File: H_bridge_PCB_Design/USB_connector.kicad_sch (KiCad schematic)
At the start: 11 parts, among them J1 TMS-102-21-G-S, P1 USB_C_Plug_USB2.0, Q7 BC817, Q8 BC817, U7 CH340C

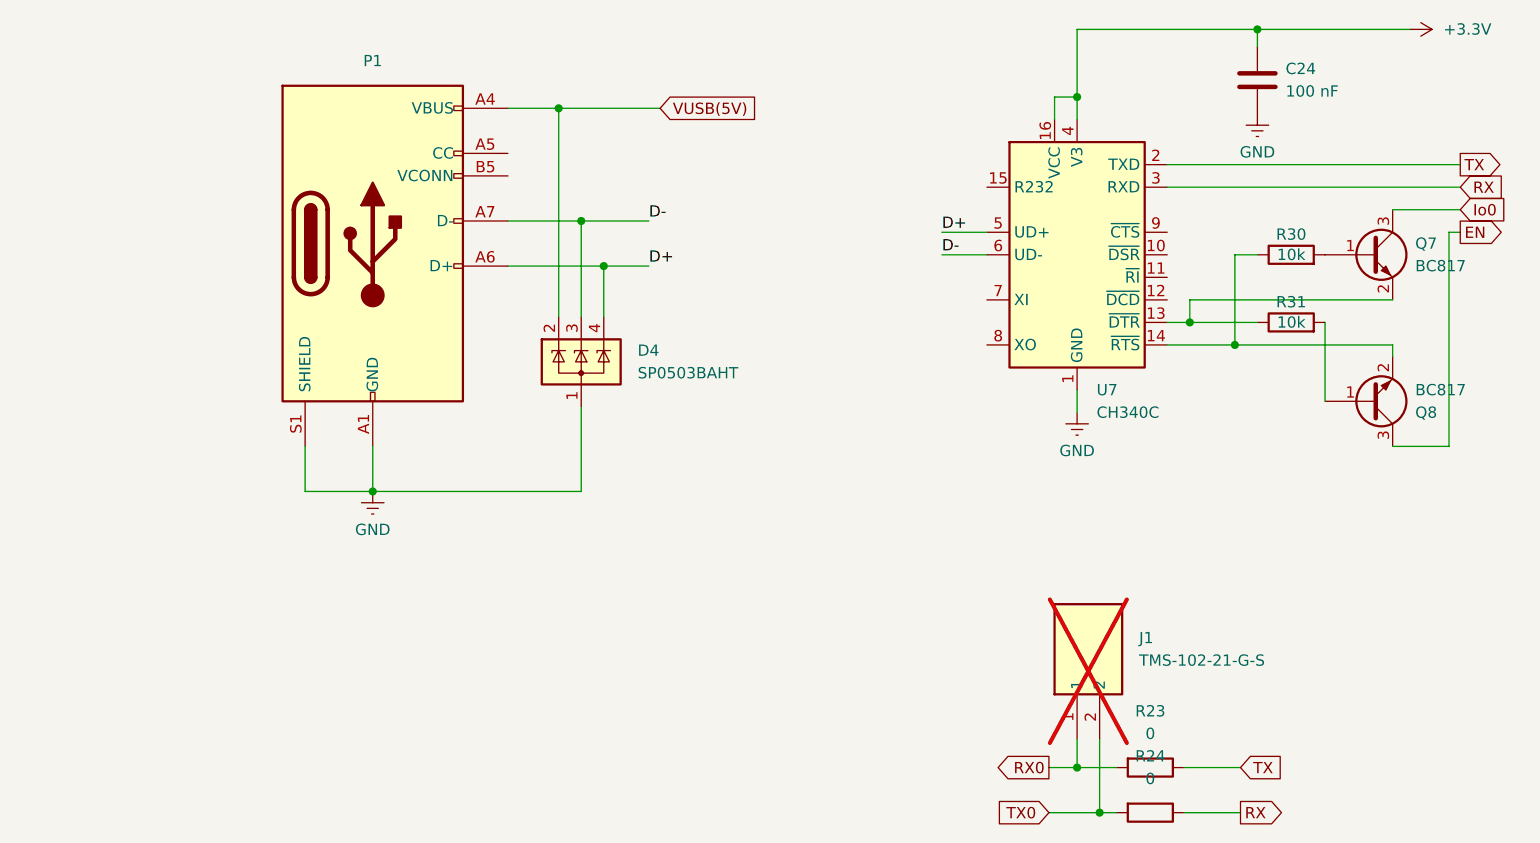
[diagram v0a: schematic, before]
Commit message: Interrupt for PWM and unipolar modulation
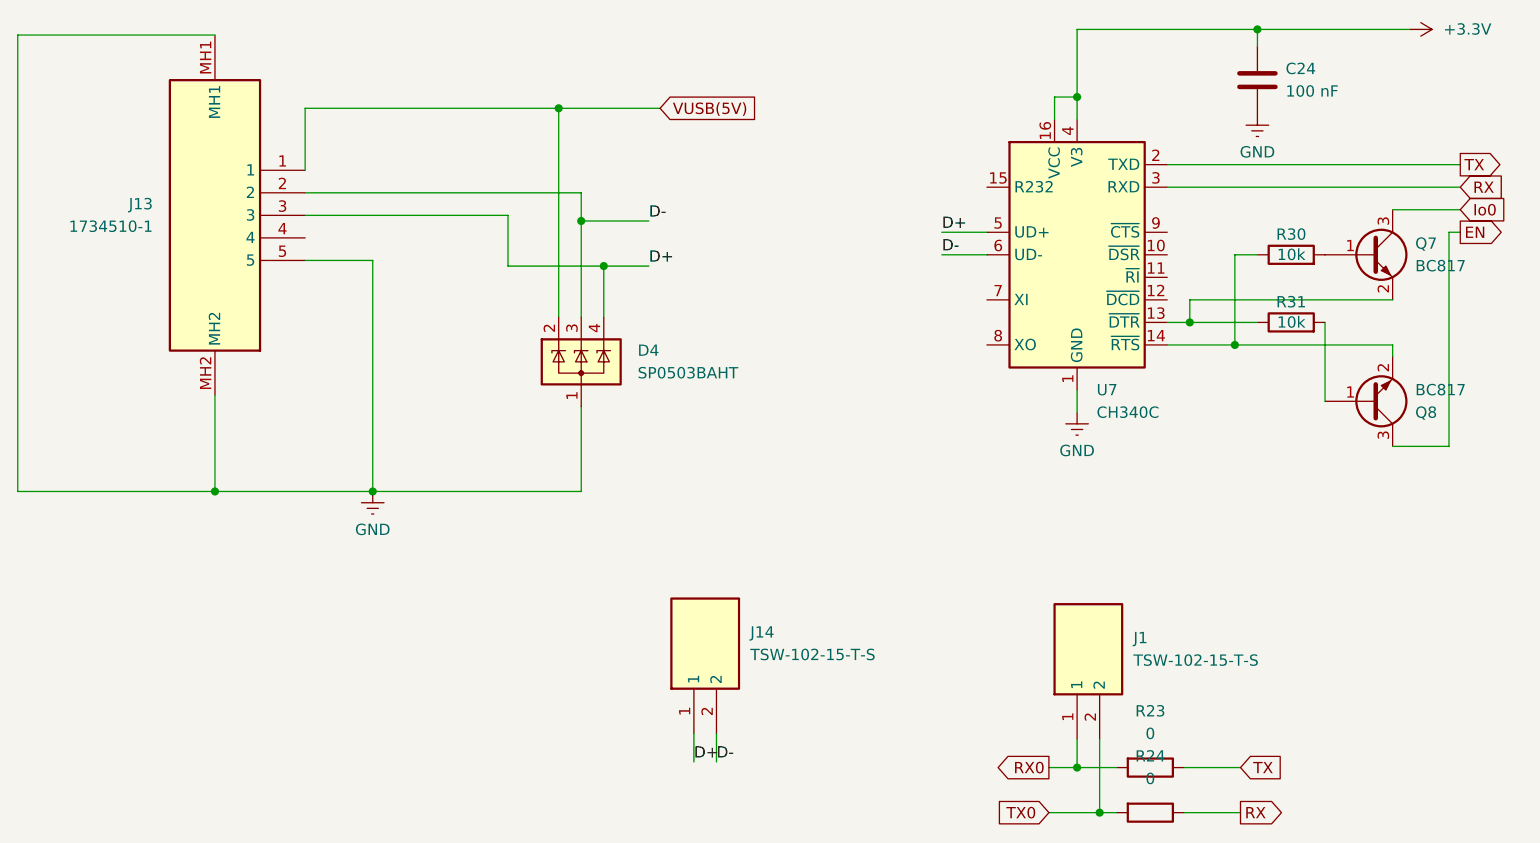
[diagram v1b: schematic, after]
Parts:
- removed J1: TMS-102-21-G-S, SamacSys_Parts:TMS-102-YY-XX-S, symbol SamacSys_Parts:TMS-102-21-G-S
- removed P1: USB_C_Plug_USB2.0, Connector_USB:USB_C_Receptacle_HCTL_HC-TYPE-C-16P-01A, symbol Connector:USB_C_Plug_USB2.0
- added J1, J14: TSW-102-15-T-S, SamacSys_Parts:TSW-102-XX-YY-S, symbol SamacSys_Parts:TSW-102-15-T-S
- added J13: 1734510-1, SamacSys_Parts:17345101, symbol SamacSys_Parts:1734510-1
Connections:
- net D+: now also J13.3, J14.1
- net D-: now also J13.2, J14.2
- net GND: now also J13.5, J13.MH1, J13.MH2
- net RX0: now also J1.1
- net TX0: now also J1.2
- net VUSB(5V): now also J13.1

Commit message: new pcb
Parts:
- C24: LCSC Part # (none) -> C49678; LCSC Part# C49678 -> (none)
- D4: LCSC Part # (none) -> C7074; LCSC Part# C7074 -> (none)
- J13: LCSC Part # (none) -> C720612
- Q7, Q8: LCSC Part # (none) -> C475629; LCSC Part# C475629 -> (none)
- R23, R24: LCSC Part # (none) -> C2074219; LCSC Part# C2074219 -> (none)
- R30, R31: LCSC Part # (none) -> C84376; LCSC Part# C84376 -> (none)
- U7: LCSC Part # (none) -> C84681; LCSC Part# C14267 -> (none)
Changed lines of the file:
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@@
 (kicad_sch
-	(version 20231120)
+	(version 20250114)
 	(generator "eeschema")
-	(generator_version "8.0")
+	(generator_version "9.0")
 	(paper "A4")
